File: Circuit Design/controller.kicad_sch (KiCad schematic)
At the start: 7 parts

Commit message: all the routing is done
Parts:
- added C44: 100nF, CoF_Capacitor:C-0402, symbol CoE_Capacitor:100nF
- added R31, R32: 10K, CoF_Resistor:R-0402, symbol CoE_Resistor:10K
- added R33, R34, R35: 22R, CoF_Resistor:R-0402, symbol CoE_Resistor:22R
- added R36: 100K, CoF_Resistor:R-0402, symbol CoE_Resistor:100K
- added R37, R39, R40: 0R, CoF_Resistor:R-0402, symbol CoE_Resistor:0R
- added R38: 18K, CoF_Resistor:R-0402, symbol CoE_Resistor:18K
- U4: renamed from U?; footprint Package_DFN_QFN:QFN-40-1EP_5x5mm_P0.4mm_EP3.8x3.8mm -> CoF_QuadFlat:QFN-40-EP
- gave numbers to parts that had none: 6
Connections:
- net +3V3: now also R31.1, R32.1
- net GND: now also C44.2, R36.2, R38.1
- net at U4.24 (ADDR2): now also R39.2
- net at U4.25 (ADDR1): now also R40.2
- net at U4.26 (SDB): now also C44.1, R35.2, R36.1
- net at U4.27 (SCL): now also R31.2, R34.2
- net at U4.28 (SDA): now also R32.2, R33.2
- net at U4.29 (ISET): now also R38.2
- net at U4.30 (SYNC): now also R37.2
- new net ADDR1: R40.1
- new net ADDR2: R39.1
- new net SCL: R34.1
- new net SDA: R33.1
- new net SDB: R35.1
- new net SYNC: R37.1

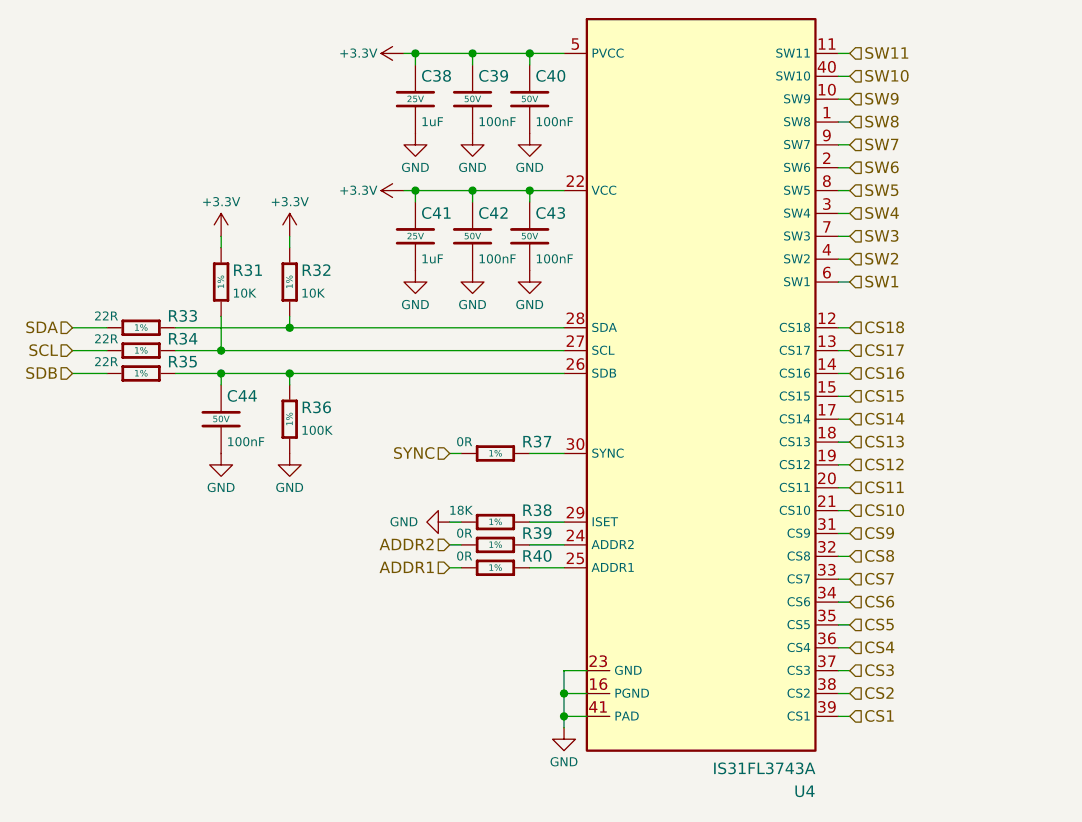
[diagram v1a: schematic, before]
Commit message: added IS31FL3731 and, edited its page
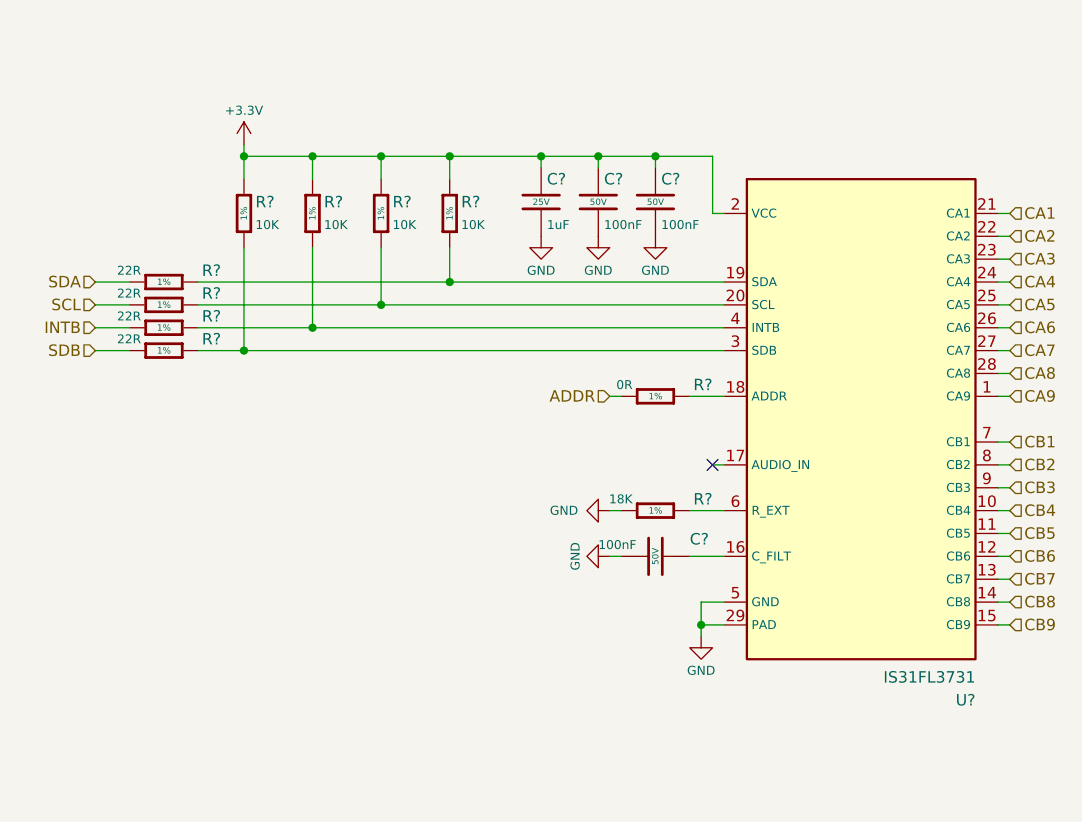
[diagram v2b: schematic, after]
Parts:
- removed C41: 1uF, CoF_Capacitor:C-0402, symbol CoE_Capacitor:1uF
- removed C42, C43, C44: 100nF, CoF_Capacitor:C-0402, symbol CoE_Capacitor:100nF
- removed R36: 100K, CoF_Resistor:R-0402, symbol CoE_Resistor:100K
- removed R37, R39: 0R, CoF_Resistor:R-0402, symbol CoE_Resistor:0R
- removed U4: IS31FL3743A, CoF_QuadFlat:QFN-40-EP, symbol CoE_IntegratedCircuit:IS31FL3743A
- added C?: 100nF, CoF_Capacitor:C-0402, symbol CoE_Capacitor:100nF
- added R? (x2): 10K, CoF_Resistor:R-0402, symbol CoE_Resistor:10K
- added R?: 22R, CoF_Resistor:R-0402, symbol CoE_Resistor:22R
- added U?: IS31FL3731, CoF_QuadFlat:QFN-28-EP, symbol CoE_IntegratedCircuit:IS31FL3731
- renumbered C40 to C?, C38 to C?, C39 to C?, R32 to R?, R31 to R?, R38 to R?, R33 to R?, R40 to R?, R35 to R?, R34 to R?
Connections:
- net +3V3: now also R?.1, R?.1, U?.2 (VCC)
- net GND: now also C?.2, U?.29 (PAD), U?.5 (GND)
- net SDB: now also R?.1; no longer R?.1
- net at R?.2: now also U?.18 (ADDR)
- net at R?.2: now also R?.2, U?.4 (INTB)
- net at R?.2, R?.2: now also U?.20 (SCL)
- net at R?.2, R?.2: now also U?.19 (SDA)
- net at R?.2: now also U?.6 (R_EXT)
- net ADDR1 renamed ADDR
- new net: R?.2, R?.2, U?.3 (SDB)
- new net: C?.1, U?.16 (C_FILT)
- new net CA1: U?.21 (CA1)
- new net CA2: U?.22 (CA2)
- new net CA3: U?.23 (CA3)
- new net CA4: U?.24 (CA4)
- new net CA5: U?.25 (CA5)
- new net CA6: U?.26 (CA6)
- new net CA7: U?.27 (CA7)
- new net CA8: U?.28 (CA8)
- new net CA9: U?.1 (CA9)
- new net CB1: U?.7 (CB1)
- new net CB2: U?.8 (CB2)
- new net CB3: U?.9 (CB3)
- new net CB4: U?.10 (CB4)
- new net CB5: U?.11 (CB5)
- new net CB6: U?.12 (CB6)
- new net CB7: U?.13 (CB7)
- new net CB8: U?.14 (CB8)
- new net CB9: U?.15 (CB9)
- new net INTB: R?.1
- no-connect marks 0 -> 1
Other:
- moved on the sheet: C?, R?

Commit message: last commit before 0805 migration
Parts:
- removed R? (x4): 22R, CoF_Resistor:R-0402, symbol CoE_Resistor:22R
- added R91, R92, R93, R94: 1R, CoF_Resistor:R-0402, symbol CoE_Resistor:1R
- U11: renamed from U?; JLCPCB Part # (none) -> C191206; Manufacturer Part # (none) -> IS31FL3731-QFLS2-TR
- gave numbers to parts that had none: 10
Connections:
- net INTB: now also R93.1
- net SCL: now also R92.1
- net SDA: now also R91.1
- net SDB: now also R94.1
- net at R87.2, U11.3 (SDB): now also R94.2
- net at R90.2, U11.19 (SDA): now also R91.2
- net at R89.2, U11.20 (SCL): now also R92.2
- net at R88.2, U11.4 (INTB): now also R93.2
- net +3V3 renamed Vin
